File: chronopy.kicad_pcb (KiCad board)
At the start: 2 copper layers, 43 x 43 mm, 77 parts, among them IC1 MCP73831T-2ACI_MC, IC2 S-1000C32-I4T1U, J1 USB_B_Micro, J2 SM02B-SRSS-TB, J3 Conn_01x04_Shielded, Q1 AO3401A, Q2 AO3401A, SW1 SW_DIP_x01, SW2 SW_DIP_x01, SW3 SW_DIP_x01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

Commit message: Some updates from the weekend
Signed-off-by: Michael Welling <mwelling@ieee.org>
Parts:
- removed MIC1: SPH0645LM4H-B, ChronoPy-PCB:SPH0645LM4H-B
- removed the Ref** at (92.7, 103.0)
- removed the Ref** at (97.0, 100.0) (x2)
- removed TFT1: DISP_TFT_1.54IN_240X240_22P, ChronoPy-PCB:0545482271
- added C17: 0.1uF, ChronoPy-PCB:C_0402, B.Cu at (137.3, 107.2)
- added J4: Conn_01x13_MountingPin, ChronoPy-PCB:Hirose_FH26W-13S-0.3SHW_2Rows-13Pins-1MP_P0.60mm, B.Cu at (116.1, 93.3)
- added J5: Conn_01x06_MountingPin, ChronoPy-PCB:Hirose_FH19C-6S-0.5SH_1x06-1MP_P0.50mm, B.Cu at (120.3, 101.5)
- added J6: Conn_02x05_Odd_Even, Connector_PinHeader_1.27mm:PinHeader_2x05_P1.27mm_Horizontal, B.Cu at (102.7, 96.3)
- added MK1: IM69D120, Sensor_Audio:Infineon_PG-LLGA-5-1, B.Cu at (138.6, 104.8)
- moved Ref** 10.2 mm to (102.0, 104.5), turned to 180 degrees
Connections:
- U3 pad 20: Net-(U3-Pad20) -> GPIO0_4
- U3 pad 21: Net-(U3-Pad21) -> GPIO0_5
- U3 pad 22: Net-(U3-Pad22) -> GPIO0_6
- U3 pad 23: Net-(U3-Pad23) -> GPIO0_7
- U3 pad 33: LCD_TE -> GPIO0_15
- U3 pad 36: Net-(U3-Pad36) -> GPIO0_21
- U3 pad 37: Net-(U3-Pad37) -> GPIO0_19
- U3 pad 42: Net-(U3-Pad42) -> GPIO0_24
- U3 pad 52: Net-(U3-Pad52) -> TS_INT
- U3 pad 53: Net-(U3-Pad53) -> TS_RST
- U3 pad 6: MIC_BCLK -> MIC_SEL
- U3 pad 7: MIC_SEL -> MIC_BCLK
- U3 pad 8: MIC_WS -> MIC_DATAOUT
- U3 pad 9: MIC_DATAOUT -> Net-(U3-Pad9)
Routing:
- net GPIO0_24: track 0.00 -> 60.2 mm, vias 0 -> 1
- net GPIO0_4: track 0.00 -> 55.4 mm, vias 0 -> 1
- net GPIO0_5: track 0.00 -> 50.9 mm, vias 0 -> 1
- net GPIO0_21: track 0.00 -> 49.1 mm, vias 0 -> 2
- net GPIO0_6: track 0.00 -> 47.6 mm, vias 0 -> 1
- net GPIO0_19: track 0.00 -> 46.7 mm, vias 0 -> 2
- net GPIO0_15: track 0.00 -> 43.5 mm, vias 0 -> 1
- net GPIO0_7: track 0.00 -> 40.9 mm, vias 0 -> 1
- net +3V0: track 16.0 -> 44.1 mm, vias 5 -> 30
- net LCD_DC: track 12.4 -> 26.5 mm
- net Net-(J4-Pad2): track 3.37 -> 16.8 mm
- net TS_INT: track 0.00 -> 12.7 mm, vias 0 -> 2
- net TS_RST: track 0.00 -> 12.6 mm, vias 0 -> 2
- net LCD_TE: track 11.3 -> 0.00 mm, vias 2 -> 0
- net MIC_BCLK: track 15.8 -> 5.91 mm
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- added copper zone on In2.Cu, net +3V0
- added copper zone on In1.Cu, net GND
- removed copper zone on B.Cu, net +3V0
- removed copper zone on F.Cu, net GND
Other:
- outline, holes or cut-outs redrawn
- copper layers 2 -> 4
- board text removed: "Designed by: Alex Camilo Michael Welling"
- board text removed: "Sponsored by: Digi-Key, SparkFun and OSHPark"

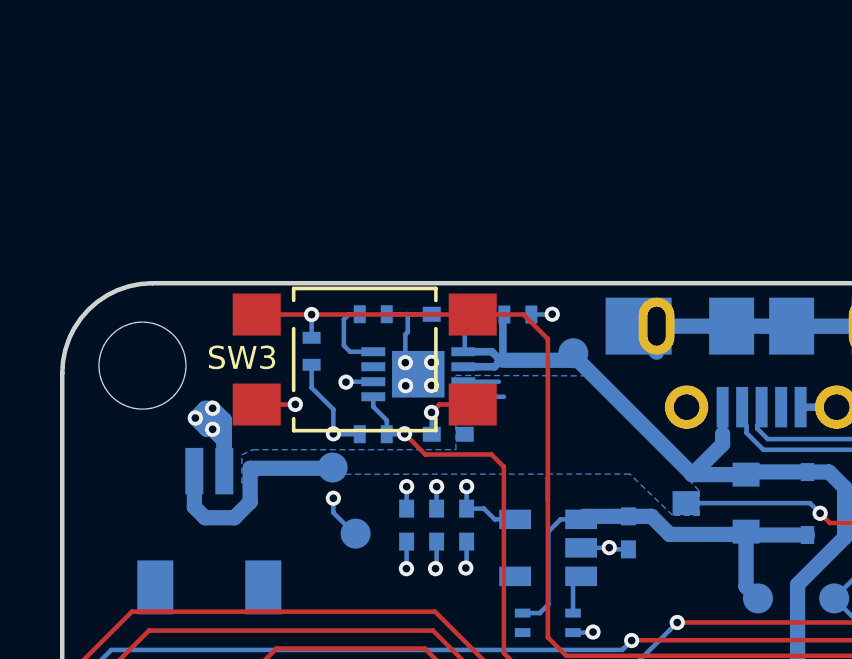
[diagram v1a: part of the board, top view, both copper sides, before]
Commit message: Clean up schematic changes for fuel gauge
Cleans schematic a bit and start the layout for the fuel gauge.

Signed-off-by: Michael Welling <mwelling@ieee.org>
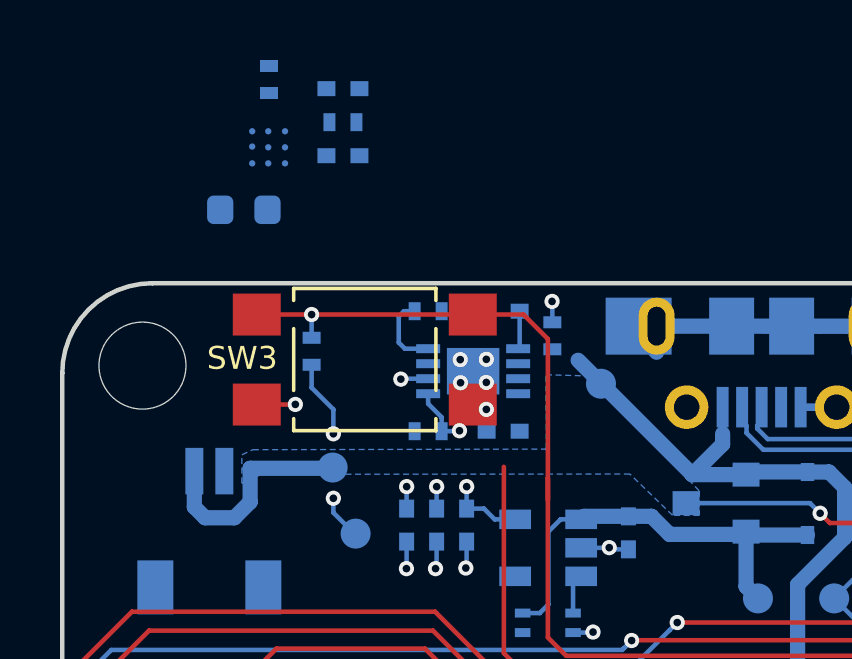
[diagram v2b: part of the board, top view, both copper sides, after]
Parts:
- added C18: 220nF, ChronoPy-PCB:C_0402, B.Cu at (108.1, 69.5)
- added C19: 1uF, ChronoPy-PCB:C_0402, B.Cu at (108.1, 71.8)
- added R21: 1k, ChronoPy-PCB:R_0402, B.Cu at (105.7, 69.2)
- added R22: 1k, ChronoPy-PCB:R_0402, B.Cu at (108.1, 70.6)
- added R23: 10m 1%, Resistor_SMD:R_0603_1608Metric, B.Cu at (104.8, 73.6)
- added U4: STC3117IJT, ChronoPy-PCB:CSP-9, B.Cu at (105.6, 71.5)
- IC2: value S-1000C32-I4T1U -> S-1000C32-I4T1U_S-1000C32-I4T1U; footprint ChronoPy-PCB:SNT-4A -> SNT-4A
- moved C3 1.83 mm to (113.5, 76.9)
- moved C5 1.83 mm to (113.5, 80.9)
- moved IC1 1.83 mm to (112.5, 78.9)
- moved R4 1.83 mm to (111.0, 76.9)
- moved R5 1.83 mm to (111.0, 80.9)
- moved TP10 1.37 mm to (116.7, 79.4)
- moved R1 1.35 mm to (115.1, 77.8), turned to 270 degrees
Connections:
- net Net-(IC1-Pad8) renamed CHG_INHB
- J2 pad 1: GND -> Net-(J2-Pad1)
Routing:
- net GND: track 85.8 -> 74.1 mm, vias 69 -> 66
- net +5P: track 38.1 -> 30.8 mm
- net CHGSTAT: track 32.8 -> 29.0 mm
- net +BATT: track 20.2 -> 17.7 mm
- net +3V0: track 44.1 -> 43.3 mm

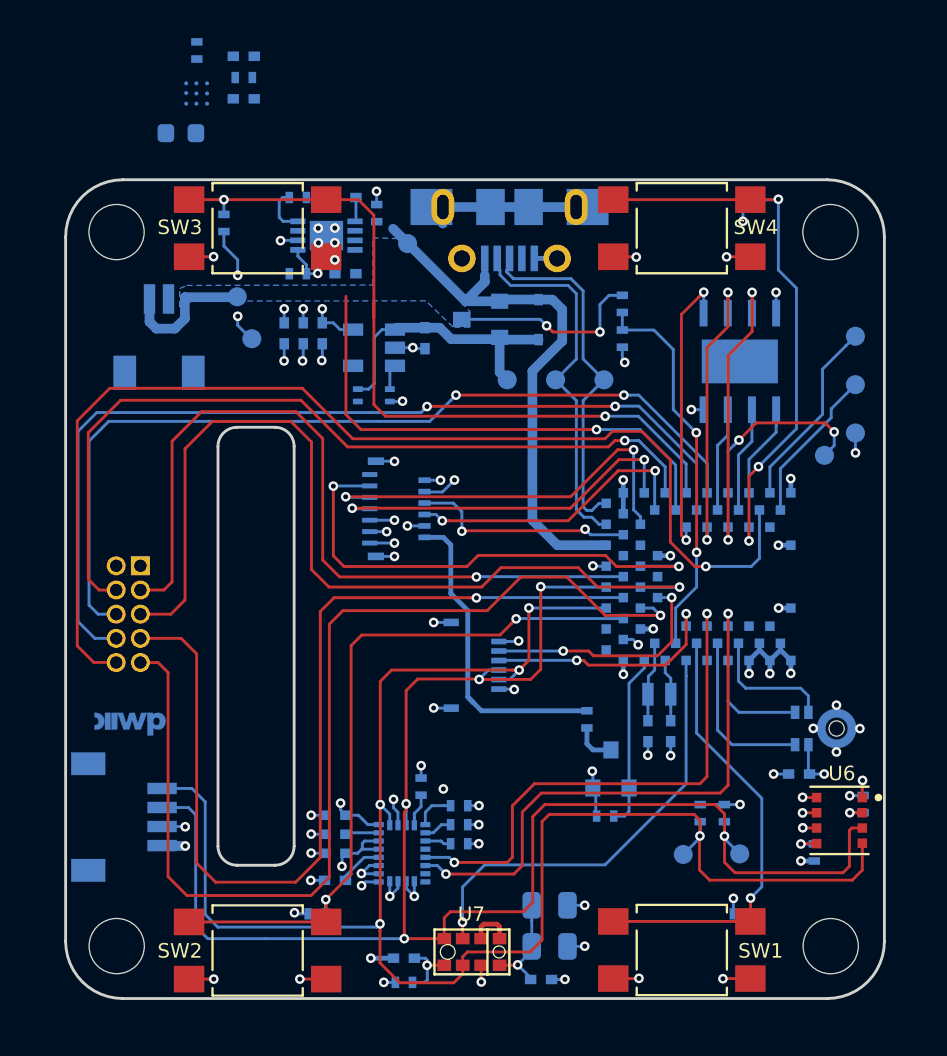
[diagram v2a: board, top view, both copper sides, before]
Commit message: Adds new fuel gauge and vibration motor
Signed-off-by: Michael Welling <mwelling@ieee.org>
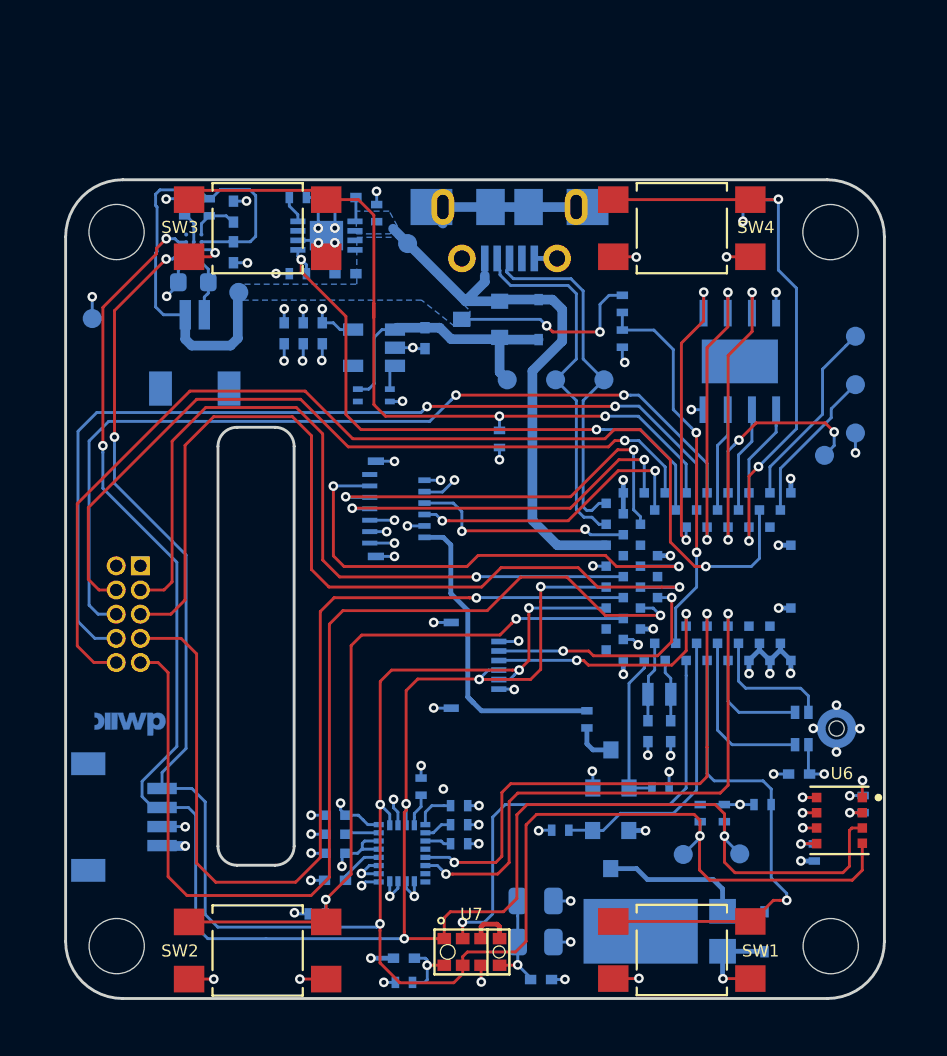
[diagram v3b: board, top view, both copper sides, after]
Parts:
- added D2: D, ChronoPy-PCB:D_SOD-323, B.Cu at (135.5, 115.5)
- added M1: Motor_DC_ALT, ChronoPy-PCB:Z43FC1B5640007L, B.Cu at (133.3, 115.5)
- added Q3: AO3401A, ChronoPy-PCB:SOT-23, B.Cu at (127.4, 111.2)
- added R24: 100k, ChronoPy-PCB:R_0402, B.Cu at (124.7, 110.2)
- U4: value STC3117IJT -> STC3115IJT; footprint ChronoPy-PCB:CSP-9 -> ChronoPy-PCB:CSP-10
- moved R2 18.4 mm to (121.5, 89.6)
- moved TP7 8.45 mm to (100.2, 83.3)
- moved R21 8.26 mm to (105.0, 77.5)
- moved C18 8.18 mm to (107.6, 77.7), turned to 90 degrees
- moved C19 8.08 mm to (107.6, 79.8), turned to 270 degrees
- moved R23 7.86 mm to (105.5, 81.4)
- moved U4 7.83 mm to (105.5, 79.3)
- moved R22 7.05 mm to (106.3, 77.5), turned to 90 degrees
- moved R7 5.84 mm to (135.4, 108.8)
- moved R8 3.27 mm to (130.0, 107.9), turned to 180 degrees
- moved J2 2.05 mm to (105.5, 85.1)
- moved C11 0.77 mm to (123.4, 113.9)
- moved C12 0.77 mm to (123.4, 116.0)
- moved TP12 0.24 mm to (107.9, 81.9)
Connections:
- IC1 pad 8: CHG_INHB -> Net-(IC1-Pad8)
- R4 pad 2: CHG_INHB -> Net-(IC1-Pad8)
- U3 pad 10: SW_A -> MOTOR_EN
- U3 pad 9: Net-(U3-Pad9) -> SW_A
- U4 pad A1: CHG_INHB -> Net-(U4-PadA1)
- U4 pad A3: GND -> Net-(C18-Pad1)
- U4 pad B1: Net-(R21-Pad1) -> IIC_SDA
- U4 pad B2: IIC_SCL -> Net-(R21-Pad1)
- U4 pad B3: Net-(J2-Pad1) -> +BATT
- U4 pad C1: Net-(C18-Pad1) -> IIC_SCL
- U4 pad C3: Net-(U4-PadC3) -> GND
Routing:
- net IIC_SDA: track 87.1 -> 122.5 mm, vias 5 -> 7
- net IIC_SCL: track 90.7 -> 123.0 mm, vias 5 -> 7
- net +BATT: track 17.7 -> 35.8 mm
- net MOTOR_EN: track 0.00 -> 15.3 mm
- net GND: track 74.1 -> 89.4 mm, vias 66 -> 68
- net Net-(D2-Pad1): track 0.00 -> 9.71 mm
- net Net-(J2-Pad1): track 0.00 -> 3.26 mm
- net GPIO0_24: track 60.2 -> 57.6 mm
- net Net-(C18-Pad1): track 0.00 -> 2.58 mm
- net CHG_INHB: track 2.54 -> 0.00 mm
- net CHGSTAT: track 29.0 -> 31.3 mm
- net GPIO0_15: track 43.5 -> 41.2 mm
- net GES_INT: track 23.2 -> 25.2 mm
- net Net-(R21-Pad1): track 0.00 -> 1.64 mm
- net Net-(IC1-Pad8): track 0.00 -> 1.44 mm
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- added copper zone on B.Cu, net +5P
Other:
- rule trace_min: 0.1524 -> 0.127

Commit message: Switch to side shooter buttons and add Tag connect
Signed-off-by: Michael Welling <mwelling@ieee.org>
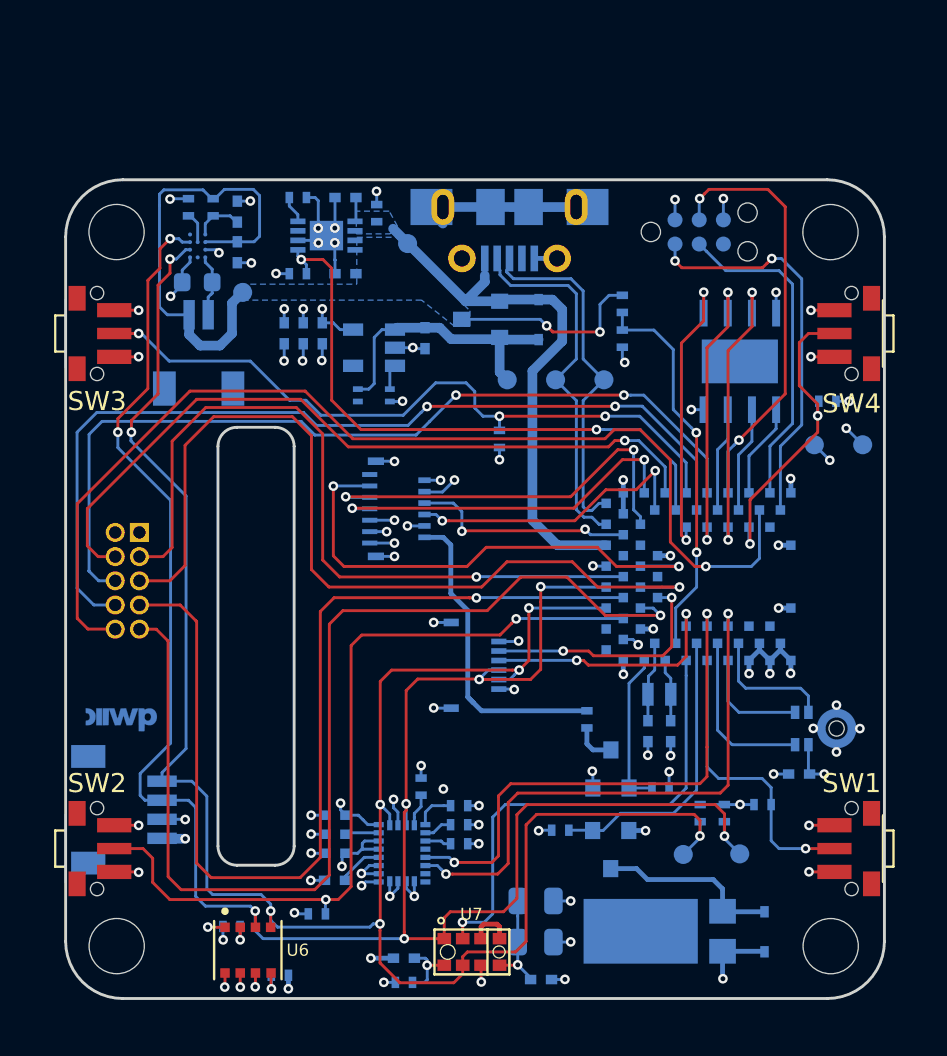
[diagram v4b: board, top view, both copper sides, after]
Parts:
- removed TP1, TP11, TP2: TestPoint, ChronoPy-PCB:Test_Point_Pad_d1.0mm
- added J7: TC2030-CTX, ChronoPy-PCB:TC2030-IDC-NL, B.Cu at (132.0, 78.7)
- M1: value Motor_DC_ALT -> Z43FC1B5640007L
- SW1, SW2, SW3, SW4: footprint ChronoPy-PCB:SW_SPST_TL3305A -> ChronoPy-PCB:SW_TL3340AF160QG
- moved TP7 38.5 mm to (138.1, 89.9), turned to 270 degrees
- moved R15 33.8 mm to (107.5, 115.2), turned to 180 degrees
- moved U6 31.8 mm to (108.3, 116.5), turned to 90 degrees
- moved R16 28.8 mm to (110.0, 117.8), turned to 0 degrees
- moved R3 11.3 mm to (138.8, 87.6), turned to 0 degrees
- moved SW4 10.5 mm to (140.0, 84.1), turned to 90 degrees
- moved SW1 10.4 mm to (140.0, 111.1), turned to 90 degrees
- moved SW3 10.1 mm to (100.4, 84.1), turned to 270 degrees
- moved SW2 9.99 mm to (100.4, 111.1), turned to 270 degrees
- moved J6 1.75 mm to (102.6, 94.5)
- moved TP9 0.73 mm to (140.6, 89.9), turned to 180 degrees
- moved Ref** 0.51 mm to (101.6, 104.3)
- moved J3 0.38 mm to (103.8, 109.1)
- moved U4 0.20 mm to (105.7, 79.3)
- moved C18 0.20 mm to (107.8, 77.7)
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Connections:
- SW1 pad 1: SW_A -> GND
- SW1 pad 2: GND -> SW_A
- SW2 pad 1: SW_B -> GND
- SW2 pad 2: GND -> SW_B
- SW3 pad 1: SW_C -> GND
- SW3 pad 2: GND -> SW_C
- SW4 pad 1: SW_D -> GND
- SW4 pad 2: GND -> SW_D
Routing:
- net SW_D: track 29.8 -> 16.2 mm, vias 3 -> 2
- net SWDIO: track 8.22 -> 20.9 mm, vias 0 -> 2
- net ~RESET: track 10.0 -> 22.5 mm
- net IIC_SCL: track 123.0 -> 110.7 mm, vias 7 -> 8
- net IIC_SDA: track 122.5 -> 111.6 mm, vias 7 -> 8
- net SW_A: track 25.4 -> 15.7 mm
- net SWCLK: track 10.1 -> 17.2 mm
- net SW_B: track 37.9 -> 42.9 mm
- net SW_C: track 41.5 -> 37.1 mm, vias 2 -> 3
- net GPIO0_15: track 41.2 -> 39.5 mm
- net GPIO0_7: track 41.2 -> 39.5 mm
- net GPIO0_24: track 57.6 -> 56.0 mm
- net GPIO0_5: track 50.9 -> 52.4 mm
- net GPIO0_6: track 48.1 -> 46.6 mm
- net GPIO0_4: track 55.4 -> 56.8 mm
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
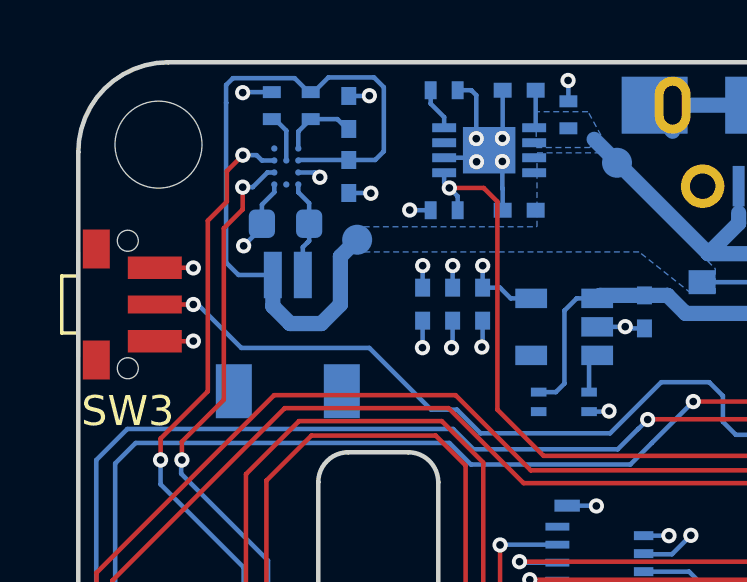
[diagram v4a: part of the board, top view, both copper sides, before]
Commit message: Tweak fuel gauge routing a bit
Signed-off-by: Michael Welling <mwelling@ieee.org>
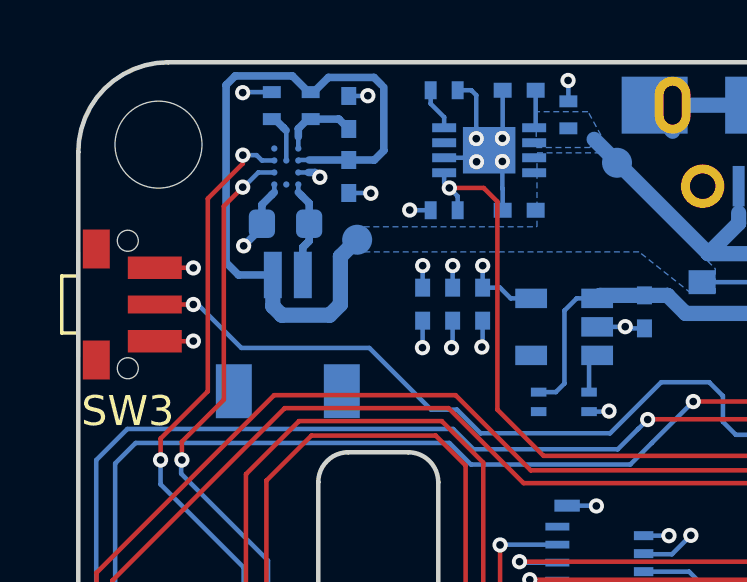
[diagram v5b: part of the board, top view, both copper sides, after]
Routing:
- net Net-(C18-Pad1): track 2.58 -> 4.04 mm
- net +BATT: track 35.2 -> 36.1 mm
